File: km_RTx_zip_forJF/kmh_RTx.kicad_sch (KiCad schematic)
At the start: 33 parts, among them IC1 ADP7118AUJZ-3.3-R7, J1 DE9_Receptacle, J3 Conn_Coaxial, J4 M80-5420442, T1 ETC4-1-2TR, U1 AD4PS-1+, U2 BD80FD0WHFP-TR, X1 3QHTF53-17.734-OE, X2 ASE-25.000MHZ-L-C-T, X3 3QHTF53-35.430-OE, X4 ASE-50.000MHZ-L-C-T

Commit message: C:\Users\khernandez\KiCad\KiCad-Project
Preliminary Part Placement
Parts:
- removed J1: DE9_Receptacle, Connector_Dsub:DSUB-9_Female_Horizontal_P2.77x2.84mm_EdgePinOffset9.40mm, symbol Connector:DE9_Receptacle
- removed J3: Conn_Coaxial, Connector_Coaxial:SMA_Amphenol_132291_Vertical, symbol Connector:Conn_Coaxial
- removed J4: M80-5420442, Connector:M80-5420442, symbol M80-5420442:M80-5420442
- added H10, H11, H12, H13, H14, H15, H16, H5, H6, H7, H8, H9: 2111-2-00-44-00-00-07-0, Turrets:2111200440000070, symbol Turrets:2111-2-00-44-00-00-07-0
- X1: footprint Oscillator:Oscillator_SMD_TXC_7C-4Pin_5.0x3.2mm -> Oscillator:Oscillator_SMD_Abracon_ASE-4Pin_3.2x2.5mm
- X3: footprint Crystal:Crystal_SMD_EuroQuartz_MJ-4Pin_5.0x3.2mm -> Oscillator:Oscillator_SMD_Abracon_ASE-4Pin_3.2x2.5mm
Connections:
- net GNDPWR: now also H15.1
- net at C13.1, C14.1, U2.4 (VO): now also H16.1
- net at R2.2: now also H14.1
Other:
- moved on the sheet: R3

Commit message: Changed the voltage regulator to a chunky SOT23 package
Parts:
- removed C10: 2.2uF, Diode_SMD:D_0805_2012Metric, symbol Device:C_Small
- removed C11: 0.1uF, Capacitor_SMD:C_0603_1608Metric, symbol Device:C_Small
- removed C9: 4.7uF, Capacitor_SMD:C_1206_3216Metric, symbol Device:C_Small
- removed H13: 2111-2-00-44-00-00-07-0, Turrets:2111200440000070, symbol Turrets:2111-2-00-44-00-00-07-0
- removed IC1: ADP7118AUJZ-3.3-R7, Package_SO:SOT95P280X100-5N, symbol ADP7118AUJZ-3_3-R7:ADP7118AUJZ-3.3-R7
- added C15: 4.7uF, Capacitor_SMD:C_1206_3216Metric, symbol Device:C_Small
- added C16: 0.1uF, Capacitor_SMD:C_0603_1608Metric, symbol Device:C_Small
- added C17: 2.2uF, Diode_SMD:D_0805_2012Metric, symbol Device:C_Small
- added IC2: UA78M33QDCYRG4Q1, LDOs:SOT230P700X180-4N, symbol SamacSys_Parts:UA78M33QDCYRG4Q1
- added R5: 100M, Resistor_SMD:R_0603_1608Metric, symbol Device:R_US
- added TP2: 3.3V, Connector_Pin:Pin_D0.7mm_L6.5mm_W1.8mm_FlatFork, symbol Connector:TestPoint
- H10: Pin # (none) -> 6
- H11: Pin # (none) -> 7
- H5: Pin # (none) -> 1
- H6: Pin # (none) -> 2
- H7: Pin # (none) -> 3
- H8: Pin # (none) -> 4
- H9: Pin # (none) -> 5
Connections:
- net +15V: now also H5.1, H6.1, C15.1, C16.1, IC2.1 (INPUT)
- net +3.3V: now also C17.1, IC2.3 (OUTPUT), TP2.1
- net GND: now also C15.2, C16.2, C17.2, IC2.2 (COMMON_1), IC2.4 (COMMON_2), R5.1
- net ReleaseAntenna: now also H7.1
- net at H11.1: now also H10.1, H8.1, H9.1, R3.2
- net at H12.1: now also R5.2
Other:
- note added: "14.3625 MHz"
- note added: "20.8875 MHz"
- note added: "29.5625 MHz"
- note added: "41.8125 MHz"
- note removed: "17.734 MHz"
- note removed: "25 MHz"
- note removed: "35.43 MHz"
- note removed: "50 MHz"
- moved on the sheet: H10, H11, H16, H5, H6, H7, H8, H9, R3

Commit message: More routing done
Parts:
- removed H12: 2111-2-00-44-00-00-07-0, Turrets:2111200440000070, symbol Turrets:2111-2-00-44-00-00-07-0
- added R10, R11, R8, R9: 0, Resistor_SMD:R_0603_1608Metric, symbol Device:R_US
- added R12: 100M, Resistor_SMD:R_0603_1608Metric, symbol Device:R_US
- added R6: 8.16k, Resistor_SMD:R_0603_1608Metric, symbol Device:R_US
- added R7: 68k, Resistor_SMD:R_0603_1608Metric, symbol Device:R_US
- added T2: ETC4-1-2TR, RF_Componets:ETC4_1_2TR, symbol ETC4-1-2TR:ETC4-1-2TR
- added TP1: 14.3625_MHz, Test_Points:5000, symbol Connector:TestPoint
- added TP3: 20.8875_MHz, Test_Points:5000, symbol Connector:TestPoint
- added TP4: 29.5625 MHz, Test_Points:5000, symbol Connector:TestPoint
- added TP5: 41.8125 MHz, Test_Points:5000, symbol Connector:TestPoint
- added TP6: SUM_OUT, Test_Points:5000, symbol Connector:TestPoint
- added TP7: GROUND, Test_Points:5000, symbol Connector:TestPoint
- C12: footprint Capacitor_SMD:C_0603_1608Metric -> Capacitor_SMD:C_1206_3216Metric
- C13: value 1uF -> 2.2uF; footprint Capacitor_SMD:C_0603_1608Metric -> Capacitor_SMD:C_1206_3216Metric
- C14: symbol Device:C_Polarized_Small_US -> Device:C
- J1: renamed from H16; value 2111-2-00-44-00-00-07-0 -> 0022232031; footprint Turrets:2111200440000070 -> Connector_PinHeader_2.54mm:PinHeader_1x03_P2.54mm_Vertical; symbol Turrets:2111-2-00-44-00-00-07-0 -> Connector:Conn_01x03_Pin; Manufacturer_Part_Number 2111-2-00-44-00-00-07-0 -> 0022232031; Mouser Part Number 575-2111200440000 -> 0022232031
- T1: footprint E_SERIES_1 -> RF_Componets:ETC4_1_2TR
- U1: footprint AD4PS1 -> RF_Componets:AD4PS1
- U2: value BD80FD0WHFP-TR -> BD00D0AWHFP-TR; footprint BD80FD0WHFPTR -> LDOs:HRP5_ROM; symbol BD80FD0WHFP-TR:BD80FD0WHFP-TR -> LDO:BD00D0AWHFP-TR
- X1: value 3QHTF53-17.734-OE -> ASSFLP-R-C02; footprint Oscillator:Oscillator_SMD_Abracon_ASE-4Pin_3.2x2.5mm -> Crystal:Crystal_SMD_Abracon_ABM3B-4Pin_5.0x3.2mm
- X2: value ASE-25.000MHZ-L-C-T -> ASSFLP-R-C02; footprint Oscillator:Oscillator_SMD_Abracon_ASE-4Pin_3.2x2.5mm -> Crystal:Crystal_SMD_Abracon_ABM3B-4Pin_5.0x3.2mm
- X3: value 3QHTF53-35.430-OE -> ASSFLP-R-C02; footprint Oscillator:Oscillator_SMD_Abracon_ASE-4Pin_3.2x2.5mm -> Crystal:Crystal_SMD_Abracon_ABM3B-4Pin_5.0x3.2mm
- X4: value ASE-50.000MHZ-L-C-T -> ASSFLP-R-C02; footprint Oscillator:Oscillator_SMD_Abracon_ASE-4Pin_3.2x2.5mm -> Crystal:Crystal_SMD_Abracon_ABM3B-4Pin_5.0x3.2mm
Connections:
- net GND: now also R12.1, R6.2, TP7.1
- net GNDPWR: now also R10.2, R11.2, R8.2, T2.3; no longer T1.3
- net at C8.1, U1.5 (PORT_4): now also TP5.1
- net at C1.1, U1.8 (PORT_1): now also TP1.1
- net at C13.1, C14.1, U2.4 (VO): now also J1.3 (Pin_3), R7.1; no longer J1.1
- net at U2.5 (ADJ): now also R6.1, R7.2
- net at R5.2: now also J1.2 (Pin_2)
- net at T1.1: now also R9.1, T2.5; no longer R2.1
- net at T1.2: now also R10.1
- net at T1.5, U1.2 (SUM_PORT): now also TP6.1
- net at C6.1, U1.6 (PORT_3): now also TP4.1
- net at C4.1, U1.7 (PORT_2): now also TP3.1
- new net: J1.1 (Pin_1), R12.2
- new net: R8.1, T1.3, T2.4
- new net: R2.1, R9.2, T2.1
- new net: R11.1, T2.2
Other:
- moved on the sheet: C1, C12, C13, C15, C16, C17, C2, C3, C4, C5, C6, C7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

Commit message: C:\Users\khernandez\KiCad\KiCad-Projects# Please enter the commit message for your changes. Lines starting
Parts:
- removed H15: 2111-2-00-44-00-00-07-0, Turrets:2111200440000070, symbol Turrets:2111-2-00-44-00-00-07-0
- removed J1: 0022232031, Connector_PinHeader_2.54mm:PinHeader_1x03_P2.54mm_Vertical, symbol Connector:Conn_01x03_Pin
- removed R11: 0, Resistor_SMD:R_0603_1608Metric, symbol Device:R_US
- removed T2: ETC4-1-2TR, RF_Componets:ETC4_1_2TR, symbol ETC4-1-2TR:ETC4-1-2TR
- added J1: Conn_01x06_Pin, Connectors_kmh:22232061, symbol Connector:Conn_01x06_Pin
- added T2: ADT16-1T+, RF_Componets:ADT161T, symbol Device:Transformer_1P_SS
- R12, R3, R4, R5: value 100M -> 10M
- R8: value 0 -> 10K
- T1: value ETC4-1-2TR -> ADT16-1T+; footprint RF_Componets:ETC4_1_2TR -> RF_Componets:ADT161T; symbol ETC4-1-2TR:ETC4-1-2TR -> Device:Transformer_1P_SS
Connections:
- net GND: now also H10.1, H11.1, H8.1, H9.1, R8.2, T1.3 (AB), J1.2 (Pin_2), J1.3 (Pin_3), J1.4 (Pin_4); no longer T1.4
- net GNDPWR: now also T1.5 (SC), T2.6 (SA); no longer R8.2
- net at R1.2, U2.1 (CTL): now also R8.1
- net at C13.1, C14.1, R7.1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: now also J1.1 (Pin_1)
- net at R12.2: now also J1.6 (Pin_6)
- net at TP6.1, U1.2 (SUM_PORT): now also T1.1 (AA); no longer T1.5
- net at R9.1: now also T1.4 (SB), T2.1 (AA); no longer T1.1
- net at R10.1: now also T1.6 (SA), T2.3 (AB); no longer T1.2
- net at R2.1, R9.2: now also T2.4 (SB)
- net at H14.1, R2.2: now also R3.2
- net at R5.2: now also J1.5 (Pin_5)
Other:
- note added: "Antenna Bleed Resistor"
- note added: "Dog House & Fangibolt Bleed Resistors"
- moved on the sheet: C1, C12, C13, C14, C2, C3, C4, C5, C6, C7, C8, H14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

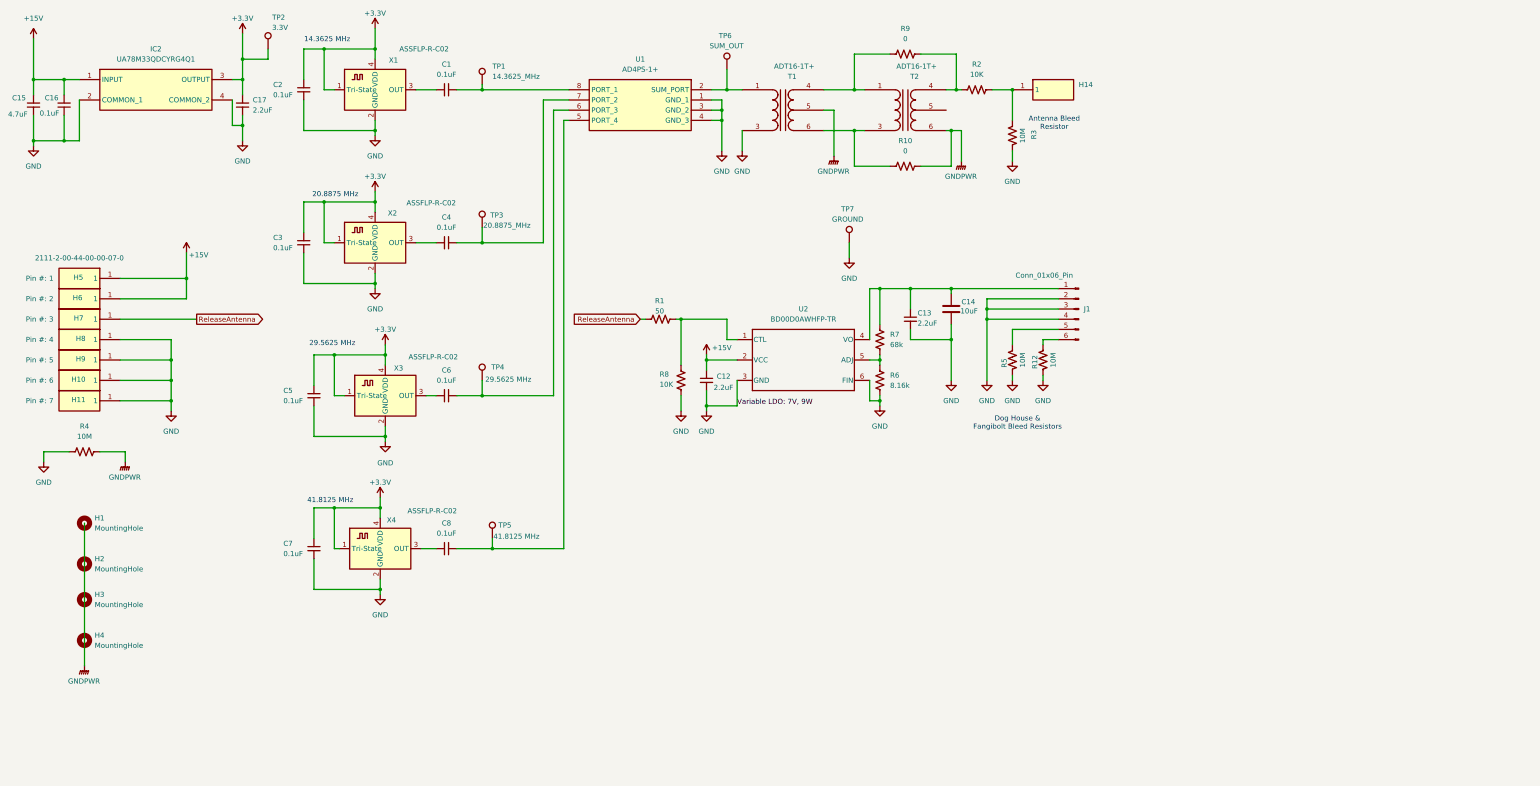
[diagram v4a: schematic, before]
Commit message: added 2 bit buffers, which replace the previous 8 bit buffers
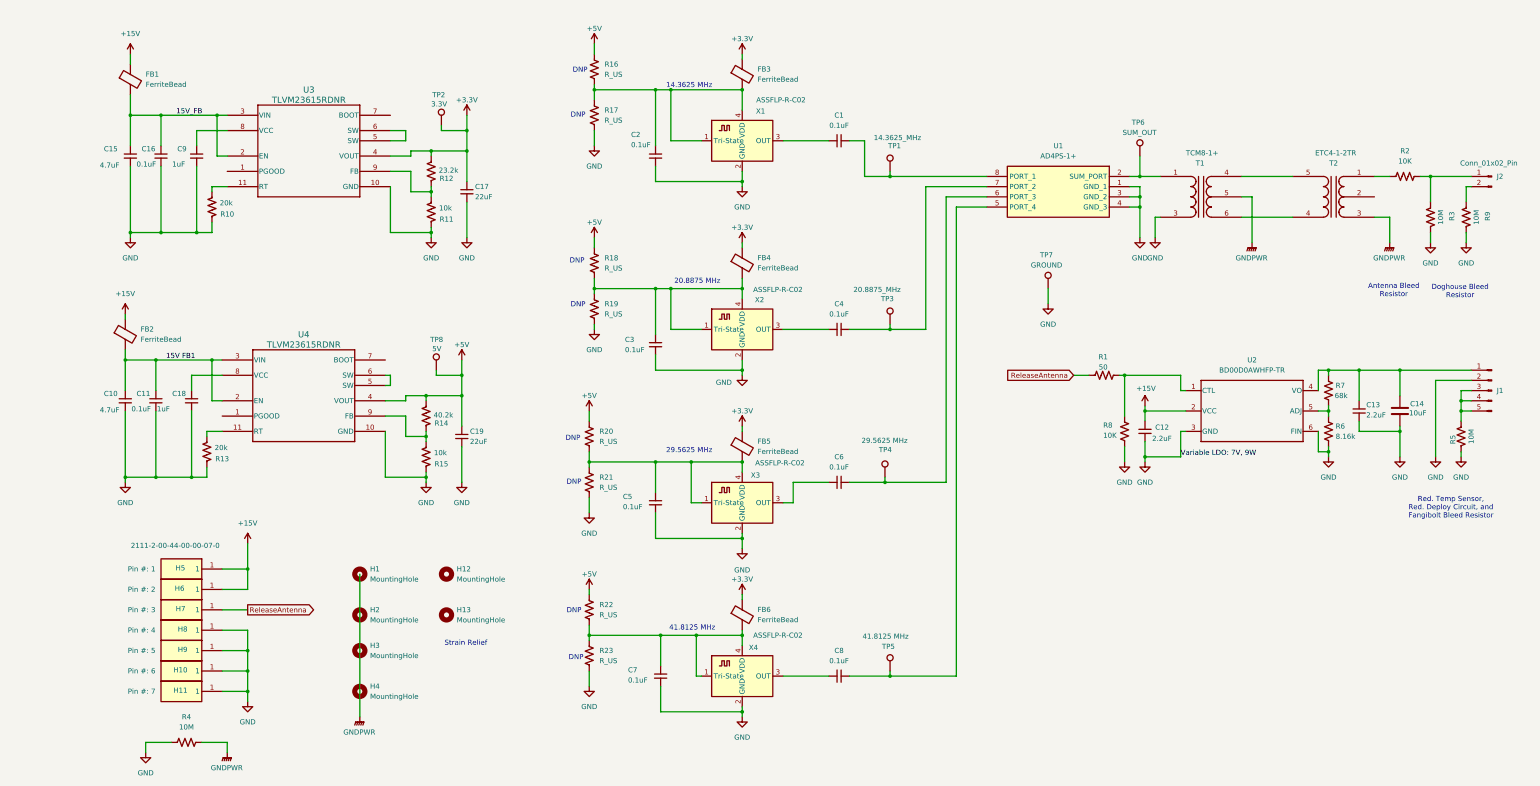
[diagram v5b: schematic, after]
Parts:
- removed H14: 2111-2-00-44-00-00-07-0, Turrets:2111200440000070, symbol Turrets:2111-2-00-44-00-00-07-0
- removed IC2: UA78M33QDCYRG4Q1, LDOs:SOT230P700X180-4N, symbol SamacSys_Parts:UA78M33QDCYRG4Q1
- added C10: 4.7uF, Capacitor_SMD:C_1206_3216Metric, symbol Device:C_Small
- added C11: 0.1uF, Capacitor_SMD:C_0603_1608Metric, symbol Device:C_Small
- added C18, C9: 1uF, Capacitor_SMD:C_0603_1608Metric, symbol Device:C_Small
- added C19: 22uF, Diode_SMD:D_0805_2012Metric, symbol Device:C_Small
- added FB1, FB2, FB3, FB4, FB5, FB6: FerriteBead, Inductor_SMD:L_0805_2012Metric, symbol Device:FerriteBead
- added H12, H13: MountingHole, MountingHole:MountingHole_2.5mm, symbol Mechanical:MountingHole
- added J2: Conn_01x02_Pin, Connectors_kmh:22232021, symbol Connector:Conn_01x02_Pin
- added R11, R15: 10k, Resistor_SMD:R_0603_1608Metric, symbol Device:R_US
- added R13: 20k, Resistor_SMD:R_0603_1608Metric, symbol Device:R_US
- added R14: 40.2k, Resistor_SMD:R_0603_1608Metric, symbol Device:R_US
- added R16, R17, R18, R19, R20, R21, R22, R23: R_US, Resistor_SMD:R_0603_1608Metric, symbol Device:R_US
- added TP8: 5V, Connector_Pin:Pin_D0.7mm_L6.5mm_W1.8mm_FlatFork, symbol Connector:TestPoint
- added U3, U4: TLVM23615RDNR, DCDC:TLVM23615, symbol TLVM23615:TLVM23615RDNR
- C17: value 2.2uF -> 22uF
- H1, H2, H3, H4: footprint MountingHole:MountingHole_2.5mm_Pad -> MountingHole:MountingHole_2.5mm
- J1: footprint Connectors_kmh:22232061 -> Connectors_kmh:22272051; symbol Connector:Conn_01x06_Pin -> Connector:Conn_01x05_Pin
- R10: value 0 -> 20k
- R12: value 10M -> 23.2k
- R9: value 0 -> 10M
- T1: value ADT16-1T+ -> TCM8-1+; footprint RF_Componets:ADT161T -> RF_Componets:TCM81; Manufacturer_Name MACOM -> Minicircuits; Manufacturer_Part_Number ETC4-1-2TR -> TCM8-1+; Mouser Part Number 937-ETC4-1-2TR -> (none); Mouser Price/Stock https://www.mouser.co.uk/ProductDetail/MACOM/ETC4-1-2TR?qs=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 -> (none)
- T2: value ADT16-1T+ -> ETC4-1-2TR; footprint RF_Componets:ADT161T -> RF_Componets:ETC4_1_2TR
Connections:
- net +15V: now also FB1.1, FB2.1; no longer C15.1, C16.1
- net +3.3V: now also R12.2, FB3.1, FB4.1, FB5.1, FB6.1, U3.4 (VOUT); no longer C2.1, C3.1, C5.1, C7.1, X1.1 (Tri-State), X1.4 (VDD), X2.1 (Tri-State), X2.4 (VDD), X3.1 (Tri-State), X3.4 (VDD), X4.1 (Tri-State), X4.4 (VDD)
- net GND: now also R10.1, R9.1, C10.2, C11.2, C18.2, C19.2, C9.2, R11.1, R13.1, R15.1, R17.2, R19.2, R21.2, R23.2, U3.10 (GND), U4.10 (GND); no longer J1.3 (Pin_3), J1.4 (Pin_4), R12.1
- net GNDPWR: now also T2.3 (SA); no longer R10.2, T2.6 (SA)
- net at R2.2, R3.2: now also J2.1 (Pin_1)
- net at T2.5 (AA): now also T1.4 (SB)
- net at J1.5 (Pin_5), R5.2: now also J1.3 (Pin_3), J1.4 (Pin_4)
- new net: C7.1, FB6.2, R22.2, R23.1, X4.1 (Tri-State), X4.4 (VDD)
- new net: R13.2, U4.11 (RT)
- new net: U4.5 (SW), U4.6 (SW)
- new net: C18.1, U4.8 (VCC)
- new net: R14.1, R15.2, U4.9 (FB)
- new net: C3.1, FB4.2, R18.2, R19.1, X2.1 (Tri-State), X2.4 (VDD)
- new net: C5.1, FB5.2, R20.2, R21.1, X3.1 (Tri-State), X3.4 (VDD)
- new net: C2.1, FB3.2, R16.2, R17.1, X1.1 (Tri-State), X1.4 (VDD)
- new net: T1.6 (SA), T2.4 (AB)
- new net: R10.2, U3.11 (RT)
- new net: R2.1, T2.1 (SB)
- new net: J2.2 (Pin_2), R9.2
- new net: R11.2, R12.1, U3.9 (FB)
- new net: U3.5 (SW), U3.6 (SW)
- new net: C9.1, U3.8 (VCC)
- new net +5V: C19.1, R14.2, R16.1, R18.1, R20.1, R22.1, TP8.1, U4.4 (VOUT)
- new net 15V FB1: C10.1, C11.1, FB2.2, U4.2 (EN), U4.3 (VIN)
- new net 15V_FB: C15.1, C16.1, FB1.2, U3.2 (EN), U3.3 (VIN)
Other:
- note added: "DNP"
- note added: "Doghouse Bleed Resistor"
- note added: "Red. Temp Sensor, Red. Deploy Circuit, and Fangibolt Bleed Resistor"
- note added: "Strain Relief"
- note removed: "Dog House & Fangibolt Bleed Resistors"
- moved on the sheet: C1, C12, C13, C14, C15, C16, C17, C2, C3, C4, C5, C6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
